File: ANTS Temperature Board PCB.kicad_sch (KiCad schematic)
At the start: 0 parts

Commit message: Initial commit
1. Schematic created
2. PICO schematic, footprint, and 3D modle added
3. ADA fruit amplifier schematic, and footprint added
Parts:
- added U1: RASPBERRY_PI_PICO, 2020RASPBERRY_PI_PICO:RASPBERRY_PI_PICO, symbol 2020RASPBERRY_PI_PICO:RASPBERRY_PI_PICO
- added U2, U3: 269, ADAFRUIT:MODULE_269, symbol ADAFRUIT:269
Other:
- title: (none) -> ANTS Thermo Board

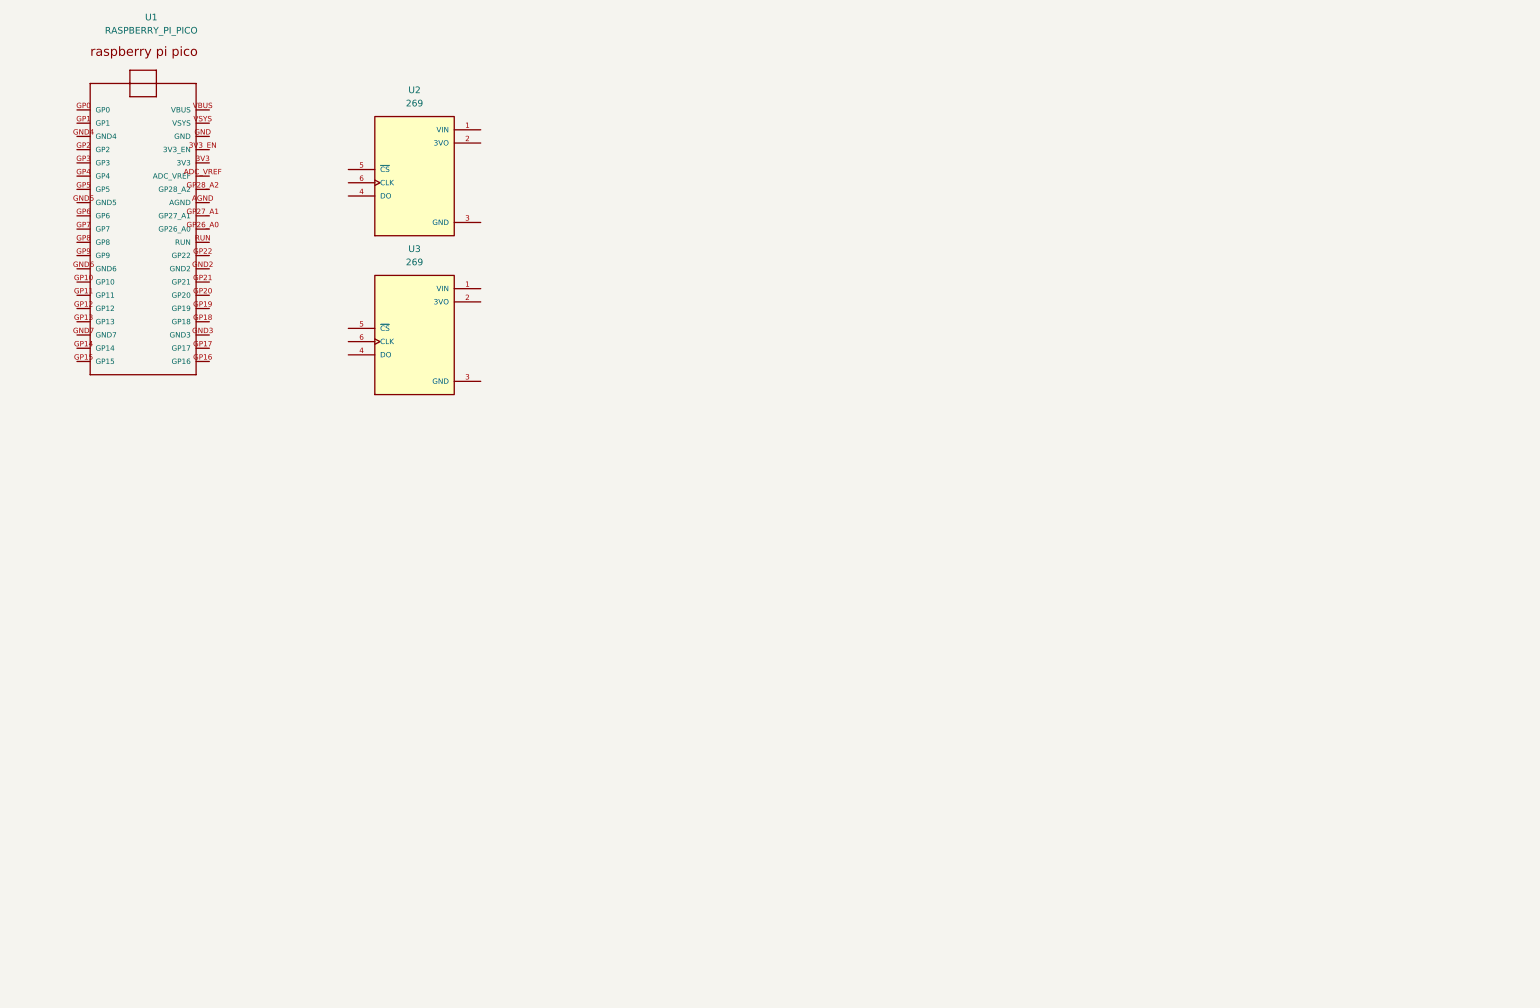
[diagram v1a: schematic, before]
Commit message: lil update
Added, terminal blocks and required resistors with the digikey link to blocks, and probes onto the schematic to make it easy to order
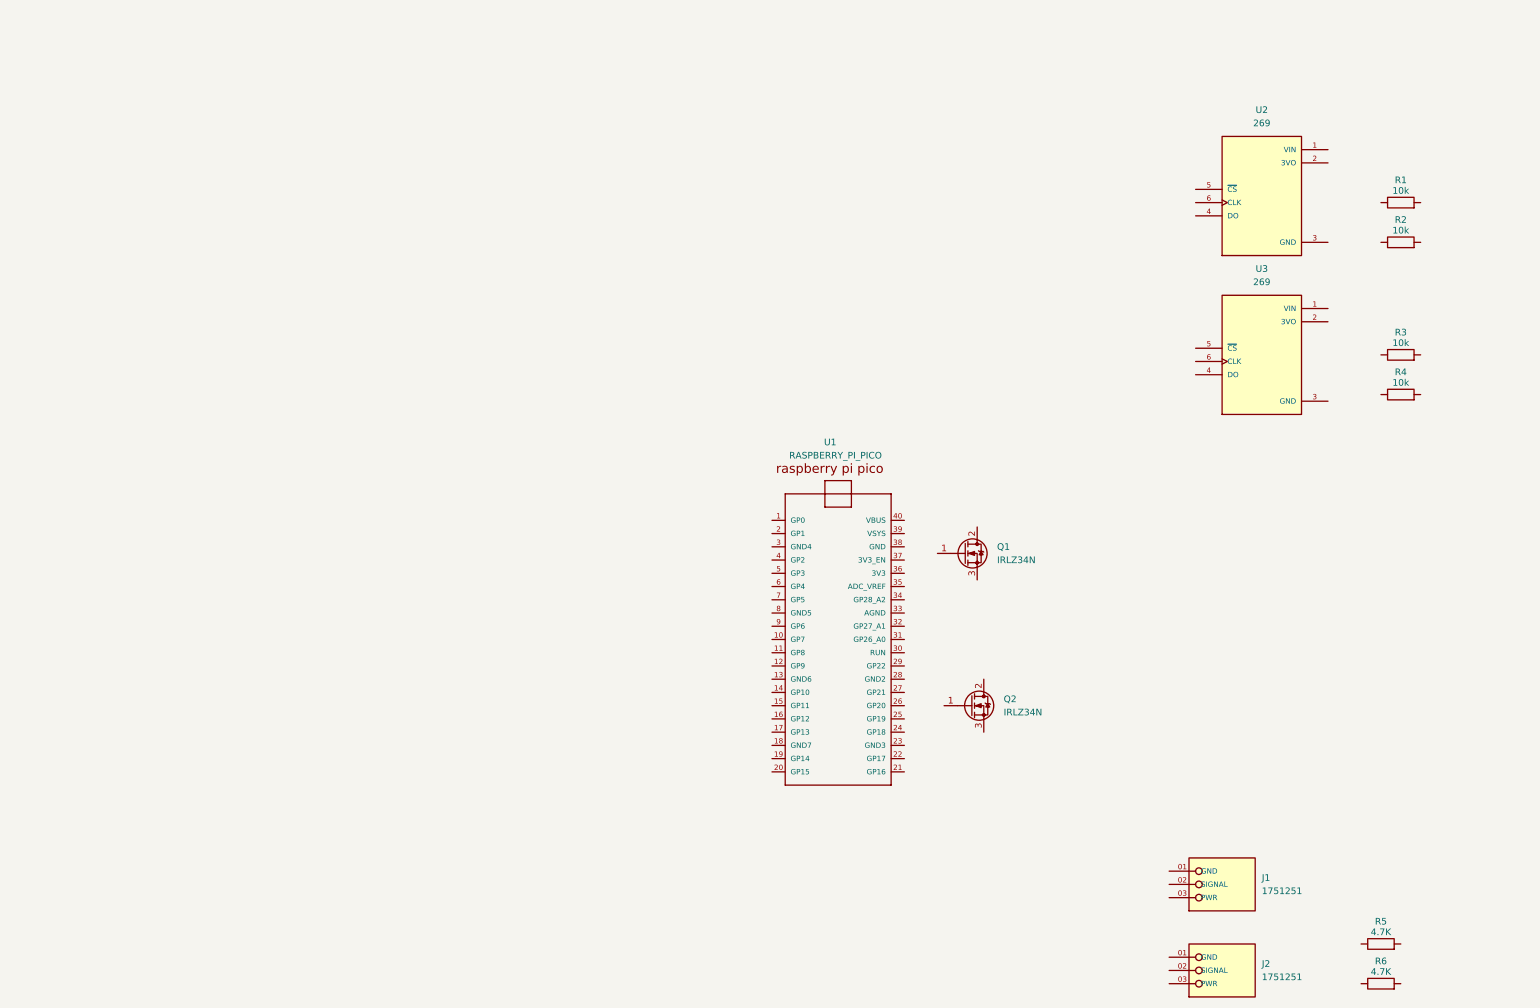
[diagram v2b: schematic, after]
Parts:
- added J1, J2: 1751251, 67TERM BLOCK:PHOENIX_1751251, symbol TERM BLOCK:1751251
- added Q1, Q2: IRLZ34N, Package_TO_SOT_THT:TO-220-3_Vertical, symbol Transistor_FET:IRLZ34N
- added R1, R2, R3, R4: 10k, symbol Device:R
- added R5, R6: 4.7K, symbol Device:R
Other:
- moved on the sheet: U1, U2, U3

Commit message: .
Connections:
- net SIGNAL2: now reaches J2.02 (SIGNAL)
- net PWR: now reaches J2.03 (PWR)
- net PWR: now also J1.03 (PWR)
- net DO01: now reaches U2.4 (DO)
- net CS01: now reaches U2.5 (~{CS})
- net CLK01: now reaches U2.6 (CLK)
- net DO02: now reaches U3.4 (DO)
- net CS02: now reaches U3.5 (~{CS})
- net CLK02: now reaches U3.6 (CLK)
- net SIGNAL: now reaches J1.02 (SIGNAL)
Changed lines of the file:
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@@
 		(comment 2 "TERM BLOCKS: https://www.digikey.com/en/models/2511152?tab=snapmagic&__cf_chl_f_tk=7YPMpYNJBV9mu8GIBdOpWFW9hMLZY80dnmunW0B23pw-1783045780-1.0.1.1-im_Ooca75lEo.MtGbQi4xqozc10oqtWe4DWxXeplAL0")
+	)
+	(wire
+		(pts
+			(xy 232.41 185.42) (xy 238.76 185.42)
+		)
+		(stroke
+			(width 0)
+			(type default)
+		)
+	)
+	(wire
+		(pts
+			(xy 231.14 201.93) (xy 238.76 201.93)
+		)
+		(stroke
+			(width 0)
+			(type default)
+		)
+	)
+	(wire
+		(pts
+			(xy 238.76 57.15) (xy 243.84 57.15)
+		)
+		(stroke
+			(width 0)
+			(type default)
+		)
+	)
+	(wire
+		(pts
+			(xy 238.76 87.63) (xy 243.84 87.63)
+		)
+		(stroke
+			(width 0)
+			(type default)
+		)
+	)
+	(wire
+		(pts
+			(xy 237.49 54.61) (xy 243.84 54.61)
+		)
+		(stroke
+			(width 0)
+			(type default)
+		)
+	)
+	(wire
+		(pts
+			(xy 238.76 52.07) (xy 243.84 52.07)
+		)
+		(stroke
+			(width 0)
+			(type default)
+		)
+	)
+	(wire
+		(pts
+			(xy 234.95 187.96) (xy 238.76 187.96)
+		)
+		(stroke
+			(width 0)
+			(type default)
+		)
+	)
+	(wire
+		(pts
+			(xy 238.76 82.55) (xy 243.84 82.55)
+		)
+		(stroke
+			(width 0)
+			(type default)
+		)
+	)
+	(wire
+		(pts
+			(xy 237.49 85.09) (xy 243.84 85.09)
+		)
+		(stroke
+			(width 0)
+			(type default)
+		)
+	)
+	(wire
+		(pts
+			(xy 233.68 199.39) (xy 238.76 199.39)
+		)
+		(stroke
+			(width 0)
+			(type default)
+		)
+	)
+	(wire
+		(pts
+			(xy 234.95 204.47) (xy 238.76 204.47)
+		)
+		(stroke
+			(width 0)
+			(type default)
+		)
+	)
+	(wire
+		(pts
+			(xy 234.95 182.88) (xy 238.76 182.88)
+		)
+		(stroke
+			(width 0)
+			(type default)
+		)
+	)
+	(label "PWR"
+		(at 234.95 187.96 0)
+		(effects
+			(font
+				(size 1.27 1.27)
+			)
+			(justify left bottom)
+		)
+	)
+	(label "DO01"
+		(at 238.76 57.15 0)
+		(effects
+			(font
+				(size 1.27 1.27)
+			)
+			(justify left bottom)
+		)
+	)
+	(label "CLK01"
+		(at 237.49 54.61 0)
+		(effects
+			(font
+				(size 1.27 1.27)
+			)
+			(justify left bottom)
+		)
+	)
+	(label "SIGNAL2"
+		(at 231.14 201.93 0)
+		(effects
+			(font
+				(size 1.27 1.27)
+			)
+			(justify left bottom)
+		)
+	)
+	(label "PWR"
+		(at 234.95 204.47 0)
+		(effects
+			(font
+				(size 1.27 1.27)
+			)
+			(justify left bottom)
+		)
+	)
+	(label "CS01"
+		(at 238.76 52.07 0)
+		(effects
+			(font
+				(size 1.27 1.27)
+			)
+			(justify left bottom)
+		)
+	)
+	(label "SIGNAL"
+		(at 232.41 185.42 0)
+		(effects
+			(font
+				(size 1.27 1.27)
+			)
+			(justify left bottom)
+		)
+	)
+	(label "CS02"
+		(at 238.76 82.55 0)
+		(effects
+			(font
+				(size 1.27 1.27)
+			)
+			(justify left bottom)
+		)
+	)
+	(label "CLK02"
+		(at 237.49 85.09 0)
+		(effects
+			(font
+				(size 1.27 1.27)
+			)
+			(justify left bottom)
+		)
+	)
+	(label "DO02"
+		(at 238.76 87.63 0)
+		(effects
+			(font
+				(size 1.27 1.27)
+			)
+			(justify left bottom)
+		)
 	)
 	(symbol

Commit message: term block 2 pin
added 2 pin term block symbol, footprint and 3D model
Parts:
- added J3, J4: EBWA-02-A, 2 PIN TERM:ADAMTECH_EBWA-02-A, symbol 2 PIN TERM:EBWA-02-A
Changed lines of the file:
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@@
+	)
+	(symbol
+		(lib_id "2 PIN TERM:EBWA-02-A")
+		(at 288.3579 140.1443 0)
+		(unit 1)
+		(exclude_from_sim no)
+		(in_bom yes)
+		(on_board yes)
+		(dnp no)
+		(fields_autoplaced yes)
+		(property "Reference" "J4"
+			(at 294.7079 140.1442 0)
+			(effects
+				(font
+					(size 1.27 1.27)
+				)
+				(justify left)
+			)
+		)
+		(property "Value" "EBWA-02-A"
+			(at 294.7079 142.6842 0)
+			(effects
+				(font
+					(size 1.27 1.27)
+				)
+				(justify left)
+			)
+		)
+		(property "Footprint" "2 PIN TERM:ADAMTECH_EBWA-02-A"
+			(at 288.3579 140.1443 0)
+			(effects
+				(font
+					(size 1.27 1.27)
+				)
+				(justify bottom)
+				(hide yes)
+			)
+		)
+		(property "Datasheet" ""
+			(at 288.3579 140.1443 0)
+			(effects
+				(font
+					(size 1.27 1.27)
+				)
+				(hide yes)
+			)
+		)
+		(property "Description" ""
+			(at 288.3579 140.1443 0)
+			(effects
+				(font
+					(size 1.27 1.27)
+				)
+				(hide yes)
+			)
+		)
+		(property "PARTREV" "A"
+			(at 288.3579 140.1443 0)
+			(effects
+				(font
+					(size 1.27 1.27)
+				)
+				(justify bottom)
+				(hide yes)
+			)
+		)
+		(property "STANDARD" "Manufacturer Recommendations"
+			(at 288.3579 140.1443 0)
+			(effects
+				(font
+					(size 1.27 1.27)
+				)
+				(justify bottom)
+				(hide yes)
+			)
+		)
+		(property "MAXIMUM_PACKAGE_HEIGHT" "8.5mm"
+			(at 288.3579 140.1443 0)
+			(effects
+				(font
+					(size 1.27 1.27)
+				)
+				(justify bottom)
+				(hide yes)
+			)
+		)
+		(property "MANUFACTURER" "AdamTech"
+			(at 288.3579 140.1443 0)
+			(effects
+				(font
+					(size 1.27 1.27)
+				)
+				(justify bottom)
+				(hide yes)
+			)
+		)
+		(pin "1"
+		)
+		(pin "2"
+		)
+		(instances
+			(project "ANTS Temperature Board PCB"
+				(path "/888122f0-519b-47ac-bd2c-ecc1a2102290"
+					(reference "J4")
+					(unit 1)
+				)
+			)
+		)
 	)
 	(symbol
@@
 		(fields_autoplaced yes)
 		(property "Reference" "U1"
-			(at 173.736 100.584 0)
+			(at 175.0772 99.06 0)
 			(effects
 				(font
@@
 		)
 		(property "Value" "RASPBERRY_PI_PICO"
-			(at 174.752 103.124 0)
+			(at 175.0772 101.6 0)
 			(effects
 				(font
@@
 					(unit 1)
 				)
+			)
+		)
+	)
+	(symbol
+		(lib_id "2 PIN TERM:EBWA-02-A")
+		(at 288.29 128.27 0)
+		(unit 1)
+		(exclude_from_sim no)
+		(in_bom yes)
+		(on_board yes)
+		(dnp no)
+		(fields_autoplaced yes)
+		(property "Reference" "J3"
+			(at 294.64 128.2699 0)
+			(effects
+				(font
+					(size 1.27 1.27)
+				)
+				(justify left)
+			)
+		)
+		(property "Value" "EBWA-02-A"
+			(at 294.64 130.8099 0)
+			(effects
+				(font
+					(size 1.27 1.27)
+				)
+				(justify left)
+			)
+		)
+		(property "Footprint" "2 PIN TERM:ADAMTECH_EBWA-02-A"
+			(at 288.29 128.27 0)
+			(effects
+				(font
+					(size 1.27 1.27)
+				)
+				(justify bottom)
+				(hide yes)
+			)
+		)
+		(property "Datasheet" ""
+			(at 288.29 128.27 0)
+			(effects
+				(font
+					(size 1.27 1.27)
+				)
+				(hide yes)
+			)
+		)
+		(property "Description" ""
+			(at 288.29 128.27 0)
+			(effects
+				(font
+					(size 1.27 1.27)
+				)
+				(hide yes)
+			)
+		)
+		(property "PARTREV" "A"
+			(at 288.29 128.27 0)
+			(effects
+				(font
+					(size 1.27 1.27)
+				)
+				(justify bottom)
+				(hide yes)
+			)
+		)
+		(property "STANDARD" "Manufacturer Recommendations"
+			(at 288.29 128.27 0)
+			(effects
+				(font
+					(size 1.27 1.27)
+				)
+				(justify bottom)
+				(hide yes)
+			)
+		)
+		(property "MAXIMUM_PACKAGE_HEIGHT" "8.5mm"
+			(at 288.29 128.27 0)
+			(effects
+				(font
+					(size 1.27 1.27)
+				)
+				(justify bottom)
+				(hide yes)
+			)
+		)
+		(property "MANUFACTURER" "AdamTech"
+			(at 288.29 128.27 0)
+			(effects
+				(font
+					(size 1.27 1.27)
+				)
+				(justify bottom)
+				(hide yes)
+			)
+		)
+		(pin "1"
+		)
+		(pin "2"
+		)
+		(instances
+			(project ""
+				(path "/888122f0-519b-47ac-bd2c-ecc1a2102290"
+					(reference "J3")
+					(unit 1)
+				)

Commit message: Pretty much finished schematic
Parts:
- removed R3, R4: 10k, symbol Device:R
- removed U2, U3: 269, ADAFRUIT:MODULE_269, symbol ADAFRUIT:269
- added J5: EBWA-02-A, 2 PIN TERM:ADAMTECH_EBWA-02-A, symbol 2 PIN TERM:EBWA-02-A
- added J6: B2B-XH-A, B2B_XH_A (1):JST_B2B-XH-A, symbol B2B-XH-A:B2B-XH-A
- added R7, R8: 220, Resistor_THT:R_Axial_DIN0204_L3.6mm_D1.6mm_P7.62mm_Horizontal, symbol Device:R
- R1, R2, R5, R6: footprint (none) -> Resistor_THT:R_Axial_DIN0204_L3.6mm_D1.6mm_P7.62mm_Horizontal
- U1: footprint 2020RASPBERRY_PI_PICO:RASPBERRY_PI_PICO -> Module:RaspberryPi_Pico_Common_THT
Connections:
- net PWR is gone; now on net +3V3: J1.03 (PWR), J2.03 (PWR)
- net SIGNAL is gone; now on net SIGNAL1: J1.02 (SIGNAL)
- net SIGNAL2: now also R6.2, U1.24 (GP18)
- net GND: now reaches J2.01 (GND)
- net GND: now also J1.01 (GND), Q1.3 (S), Q2.3 (S), R1.2, R2.2, U1.13 (GND6), U1.18 (GND7), U1.23 (GND3), U1.28 (GND2), U1.3 (GND4), U1.38 (GND), U1.8 (GND5), J5.2
- net +3V3: now reaches R6.1
- net +3V3: now also R5.1, U1.36 (3V3)
- net +7.5V: now reaches J4.1 (PWR)
- net +7.5V: now also J3.1
- net at J4.2 (Drain): now also Q2.2 (D)
- net SIGNAL1: now reaches R5.2
- net SIGNAL1: now also U1.25 (GP19)
- net at Q2.1 (G): now also R2.1, R8.2
- net at Q1.1 (G): now also R1.1, R7.2
- net at Q1.2 (D): now also J3.2
- net UART_TX: now reaches U1.1 (GP0)
- net UART_TX: now also J6.2
- net UART_RX: now reaches U1.2 (GP1)
- net UART_RX: now also J6.1
- net mosfet2_gate: now reaches U1.32 (GP27_A1)
- net mosfet2_gate: now also R8.1
- net mosfet1_gate: now reaches U1.34 (GP28_A2)
- net mosfet1_gate: now also R7.1
- net VSYS: now reaches U1.39 (VSYS)
- net VSYS: now also J5.1
- no-connect marks 0 -> 25
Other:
- moved on the sheet: J1, J2, J3, J4, Q1, Q2, R1, R2, R5, R6, U1

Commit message: No major new changes.
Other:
- moved on the sheet: J1, J2, J3, J4, J5, J6, Q1, Q2, R1, R2, R5, R6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

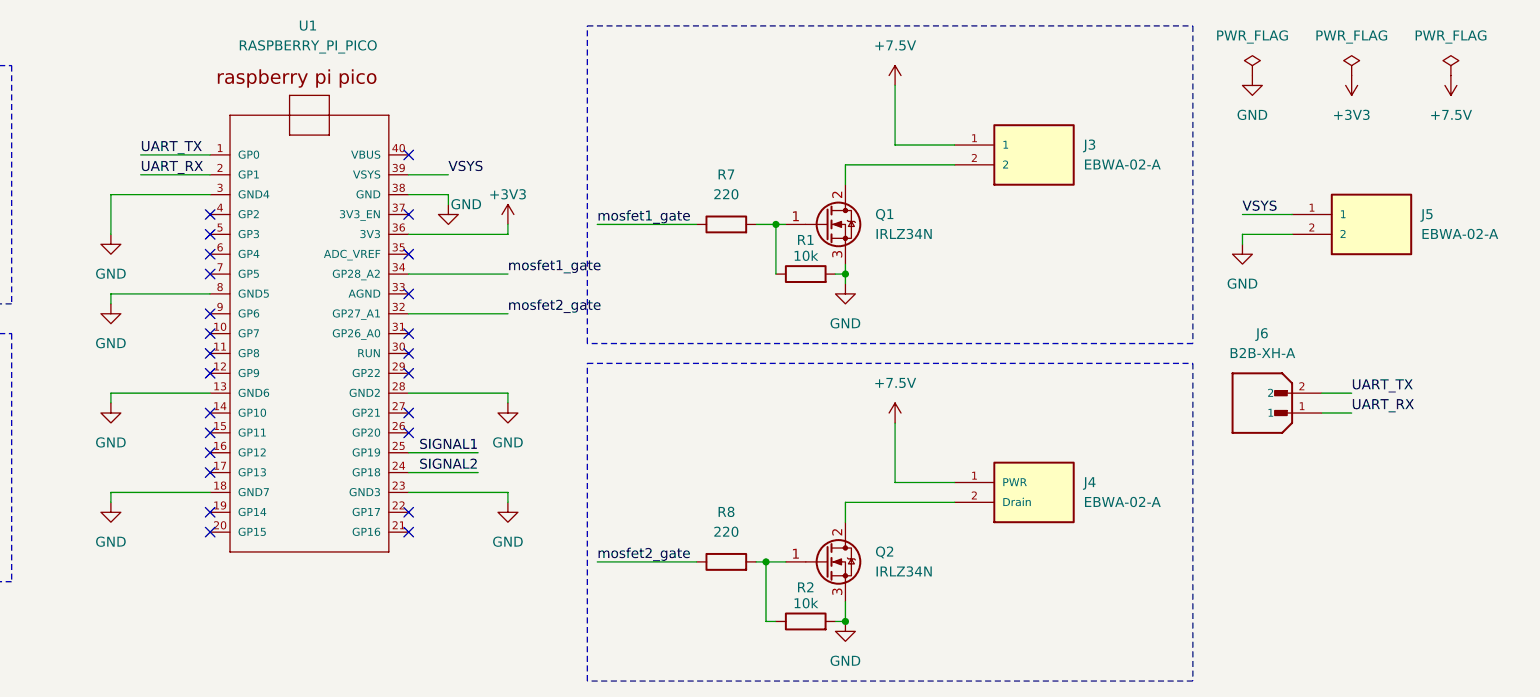
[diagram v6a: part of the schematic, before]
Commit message: Extra push for schematic changes. Only small changes to make board layout cleaner.
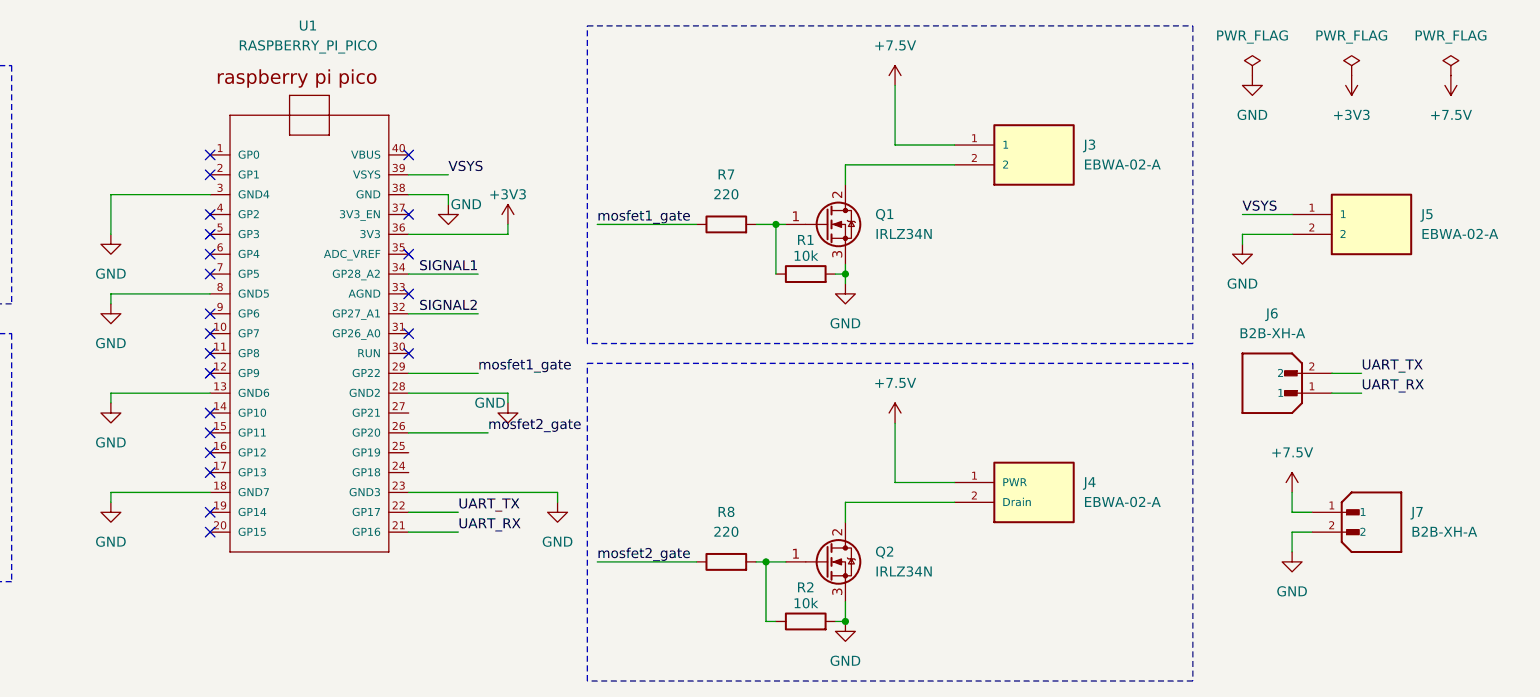
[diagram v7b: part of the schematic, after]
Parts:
- added J7: B2B-XH-A, B2B_XH_A (1):JST_B2B-XH-A, symbol B2B-XH-A:B2B-XH-A
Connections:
- net +7.5V: now also J7.1
- net GND: now also J7.2
- net SIGNAL1: now also U1.34 (GP28_A2); no longer U1.25 (GP19)
- net SIGNAL2: now also U1.32 (GP27_A1); no longer U1.24 (GP18)
- net UART_RX: now also U1.21 (GP16); no longer U1.2 (GP1)
- net UART_TX: now also U1.22 (GP17); no longer U1.1 (GP0)
- net mosfet1_gate: now also U1.29 (GP22); no longer U1.34 (GP28_A2)
- net mosfet2_gate: now also U1.26 (GP20); no longer U1.32 (GP27_A1)
- no-connect marks 25 -> 22
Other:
- moved on the sheet: J6

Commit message: Added Mounting Holes
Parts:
- added H1, H2, H3, H4: MountingHole_Pad, MountingHole:MountingHole_2.5mm_Pad_Via, symbol Mechanical:MountingHole_Pad
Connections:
- net GND: now also H1.1, H2.1, H3.1, H4.1
- net UART_RX: now also U1.22 (GP17); no longer U1.21 (GP16)
- net UART_TX: now also U1.21 (GP16); no longer U1.22 (GP17)
- no-connect marks 22 -> 25
